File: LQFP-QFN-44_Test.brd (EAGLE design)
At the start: 28.9 x 21.6 mm, 6 parts

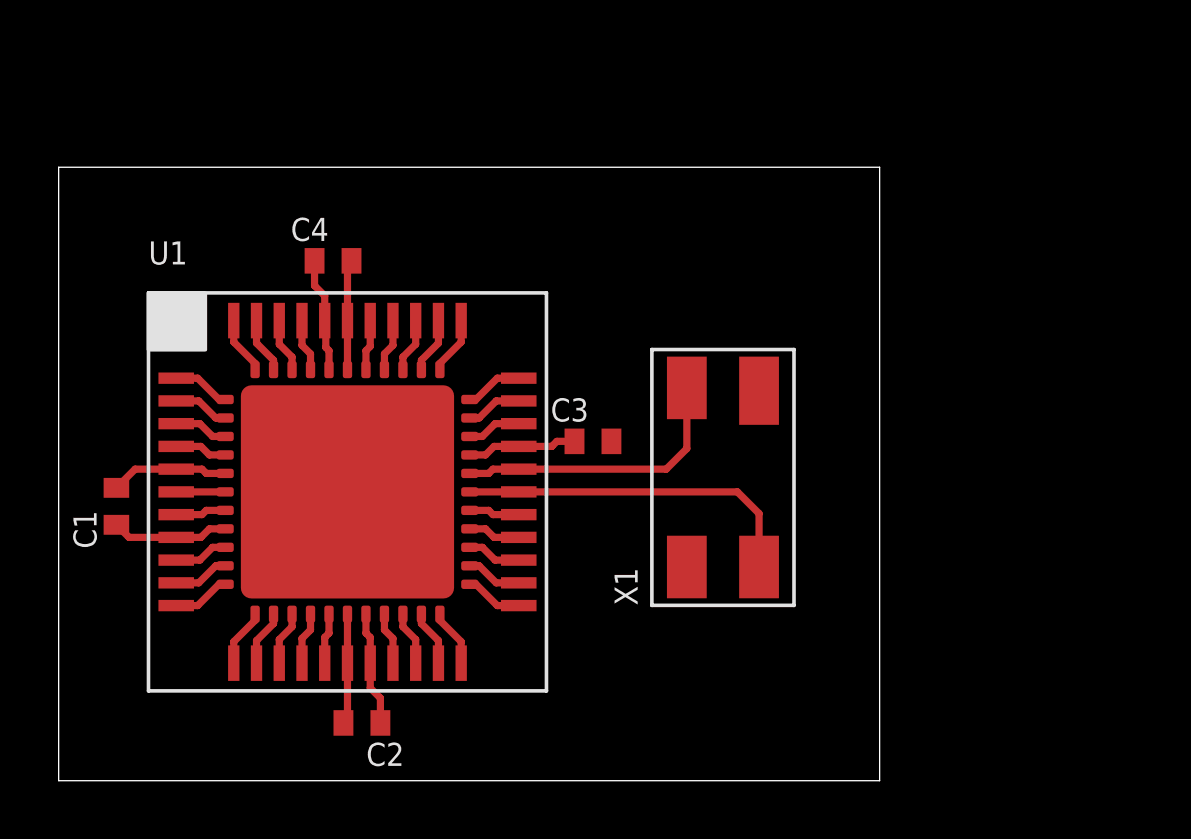
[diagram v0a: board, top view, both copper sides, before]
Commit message: Finished the layout for the appnote.
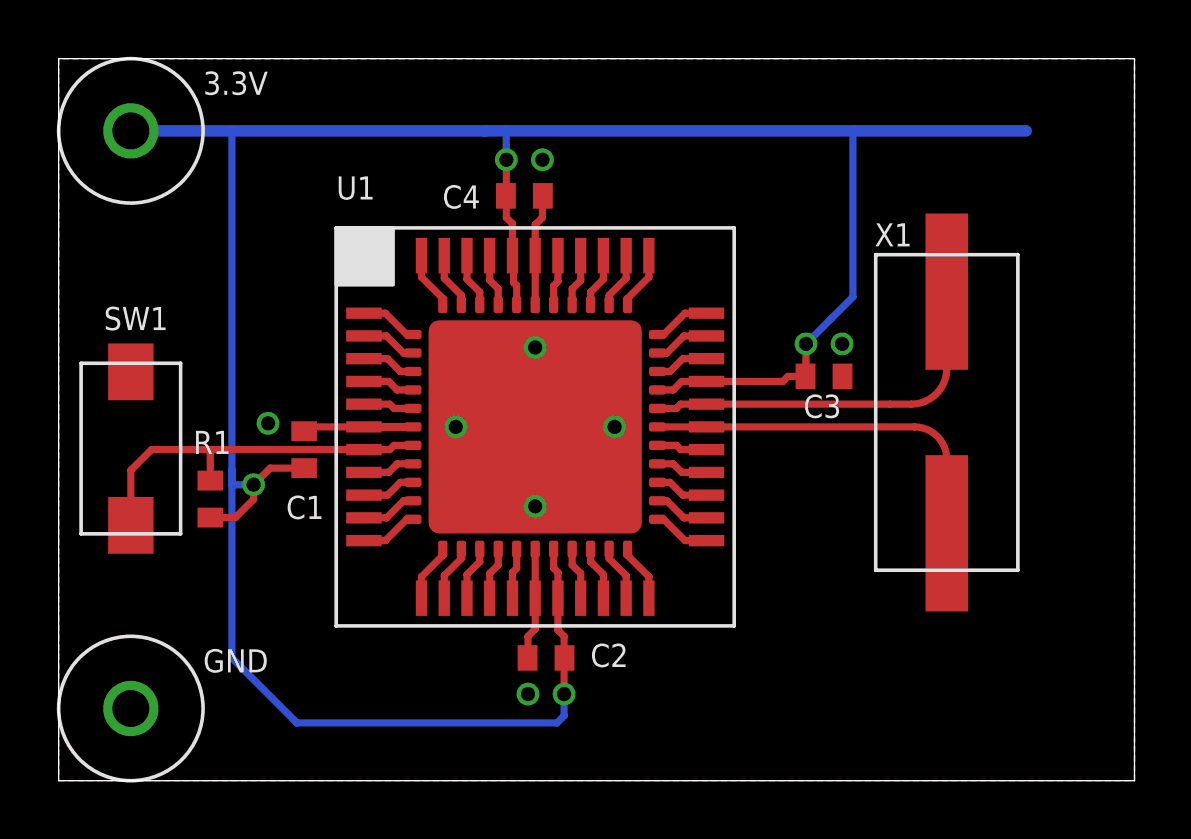
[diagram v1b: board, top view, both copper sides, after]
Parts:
- added 3.3V, GND: 5115-5119, PP_Connectors:KEYSTONE_5115-5119
- added R1: 10K, PP_Passives:0402
- added SW1: 101-0134-EV, PP_Electromechanical:101-0134-EV
- C1, C2, C3, C4: value (none) -> 0.1uF
- U1: value (none) -> P8X32A
- X1: value (none) -> ATS060CSM-1; device PP_FreqCtrl:7MM_X_5MM -> PP_FreqCtrl:HC-49/US_SM
- moved C3 8.44 mm to (26.9, 14.2)
- moved X1 8.20 mm to (31.2, 13.0)
- moved C4 7.11 mm to (16.4, 20.6)
- moved U1 6.99 mm to (16.8, 12.4)
- moved C1 6.90 mm to (8.64, 11.6)
- moved C2 6.87 mm to (17.1, 4.32)
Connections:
- net N$10 renamed P7
- net N$11 renamed P8
- net N$12 renamed P9
- net N$13 renamed P10
- net N$14 renamed P11
- net N$15 renamed P12
- net N$16 renamed P13
- net N$17 renamed P14
- net N$18 renamed P15
- net N$22 renamed P31
- net N$23 renamed P30
- net N$24 renamed P29
- net N$25 renamed P28
- net N$26 renamed P27
- net N$27 renamed P26
- net N$28 renamed P25
- net N$29 renamed P24
- net N$3 renamed P0
- net N$30 renamed P23
- net N$32 renamed P16
- net N$33 renamed P17
- net N$34 renamed P18
- net N$35 renamed P19
- net N$36 renamed P20
- net N$37 renamed P21
- net N$38 renamed P22
- net N$4 renamed P1
- net N$5 renamed P2
- net N$6 renamed P3
- net N$7 renamed P4
- net N$8 renamed P5
- net N$9 renamed P6
- removed net N$1: U1.50, U1.6
- removed net N$2: U1.51, U1.7
- removed net N$20: U1.29, U1.73, X1.3
- removed net N$21: U1.28, U1.72, X1.1
- new net RES: R1.1, SW1.2, U1.51, U1.7
- new net X0: U1.29, U1.73, X1.P$2
- new net X1: U1.28, U1.72, X1.P$1
- net 3.3V: now also 3.3V.P$1, R1.2
- net GND: now also GND.P$1, SW1.1, U1.50, U1.6
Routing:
- net 3.3V: track 16.1 -> 98.3 mm, vias 0 -> 4
- net X0: track 0.00 -> 13.5 mm
- net RES: track 0.00 -> 13.3 mm
- net X1: track 0.00 -> 13.3 mm
- net N$21: track 12.4 -> 0.00 mm
- net N$20: track 10.1 -> 0.00 mm
- net GND: track 13.7 -> 17.1 mm, vias 0 -> 8
- net N$2: track 1.79 -> 0.00 mm
- net N$1: track 1.73 -> 0.00 mm
- added copper zone on layer 1, net GND
- added copper zone on layer 16, net GND
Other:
- board size 28.9 x 21.6 mm -> 37.8 x 25.4 mm
